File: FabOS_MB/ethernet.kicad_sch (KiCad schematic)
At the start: 42 parts, among them J1 RJ45, U4 LAN8742A, U5 USBLC6-4SC6, U6 CND-tek B1601S

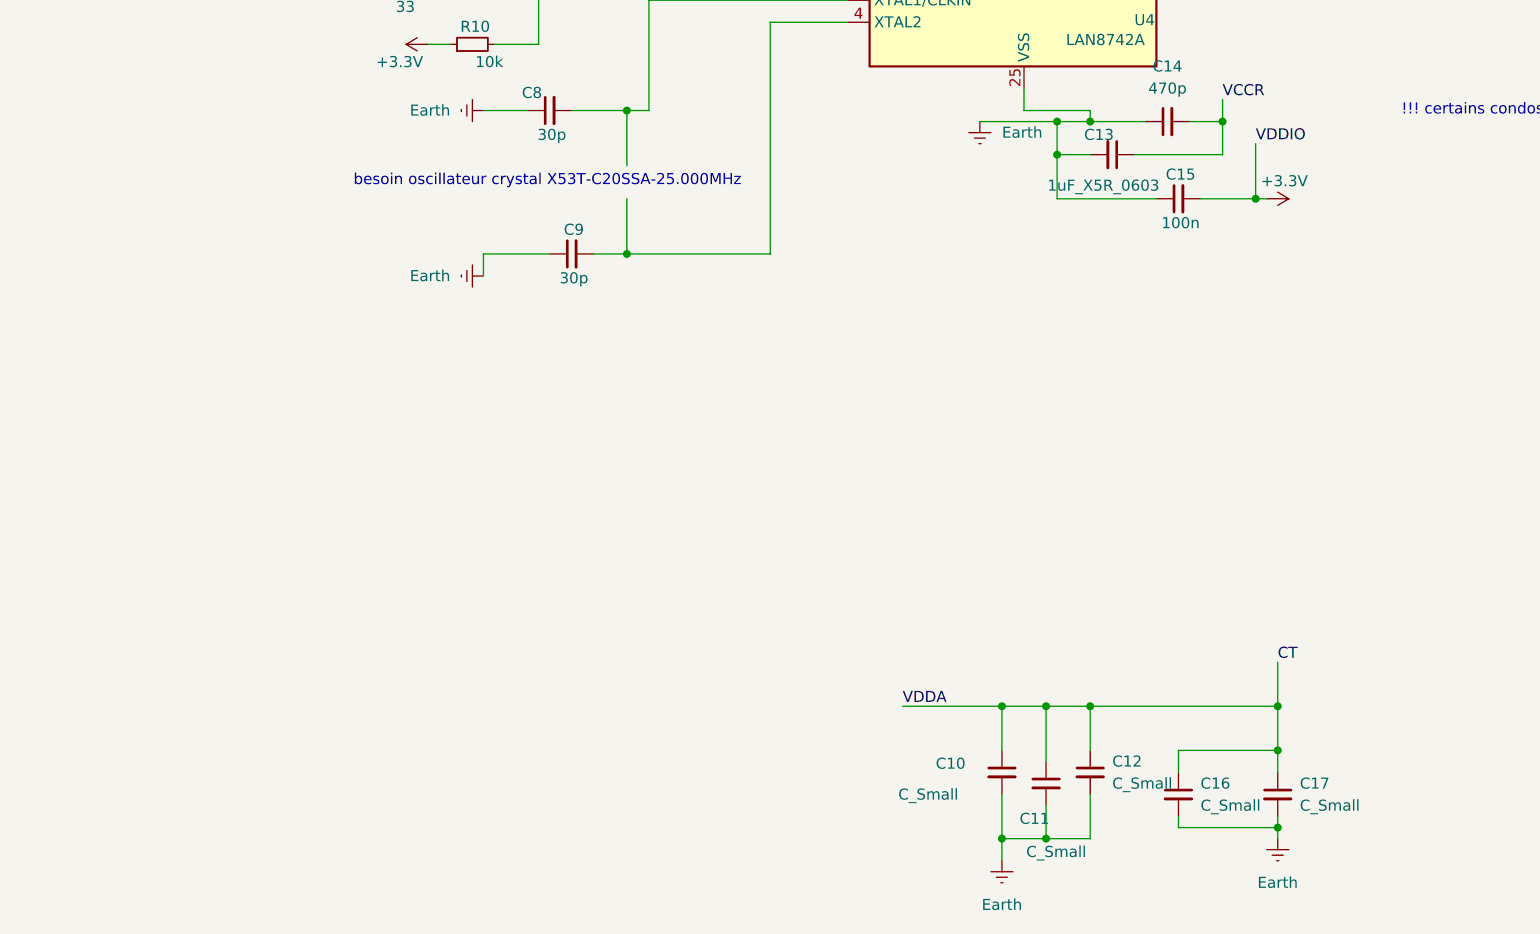
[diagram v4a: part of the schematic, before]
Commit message: ajout nom des composants pour 5v
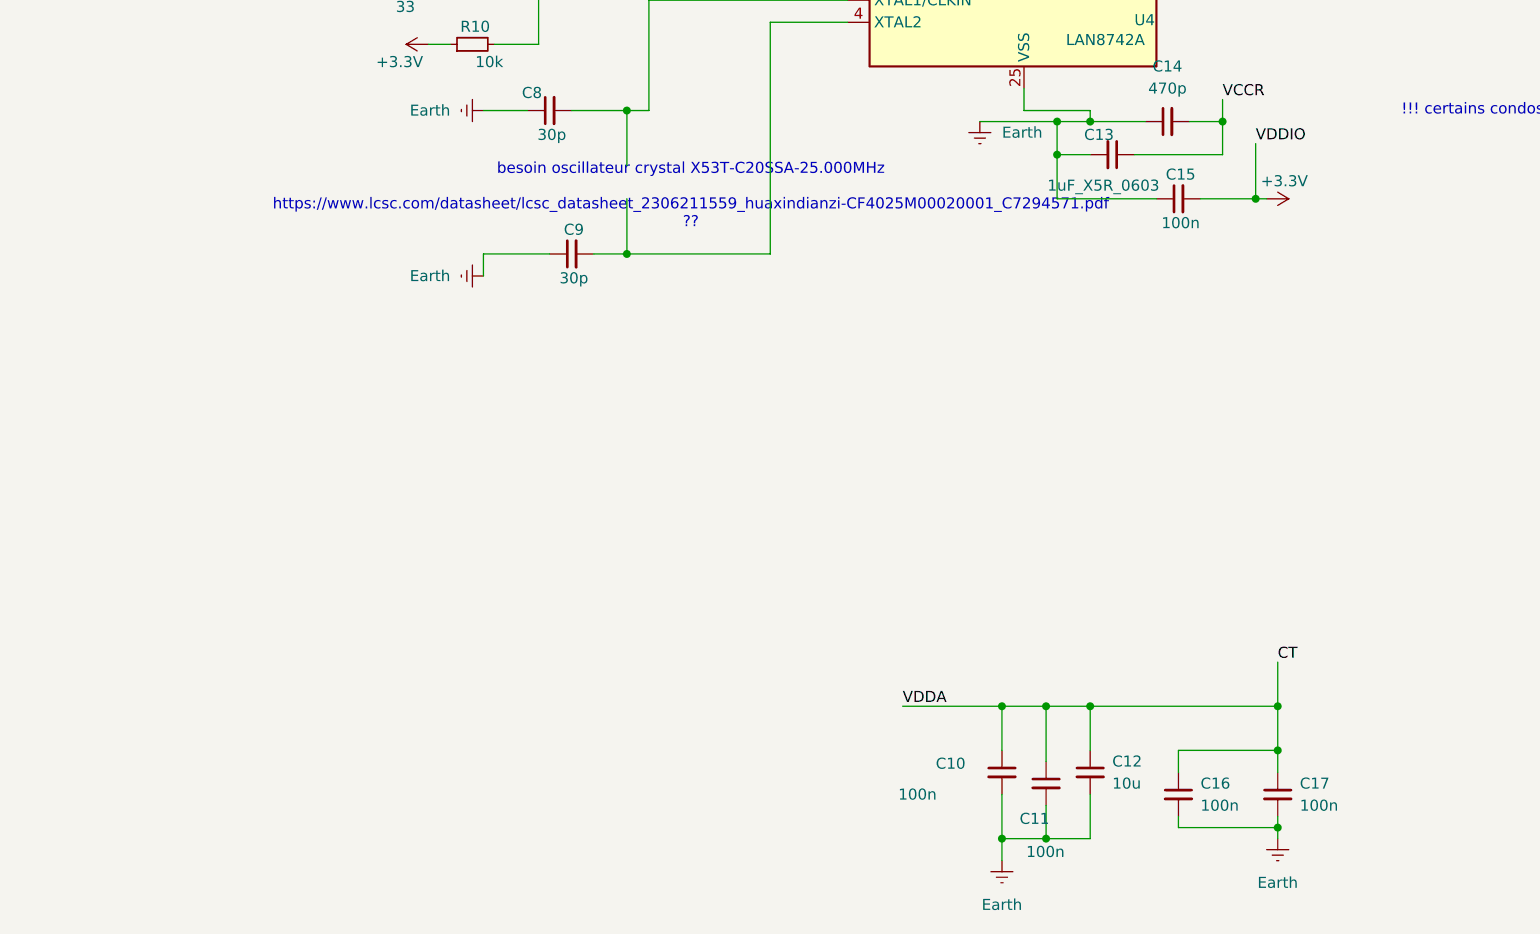
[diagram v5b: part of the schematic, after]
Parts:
- C10, C11, C16, C17: value C_Small -> 100n
- C12: value C_Small -> 10u
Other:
- note added: "besoin oscillateur crystal X53T-C20SSA-25.000MHz https://www.lcsc.com/datasheet/lcsc_datasheet_2306211559_huaxindianzi-CF4025M00020001_C7294571.pdf ??"
- note removed: "besoin oscillateur crystal X53T-C20SSA-25.000MHz"
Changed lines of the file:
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@@
 		)
 	)
-	(text "besoin oscillateur crystal X53T-C20SSA-25.000MHz"
+	(text "besoin oscillateur crystal X53T-C20SSA-25.000MHz\n\nhttps://www.lcsc.com/datasheet/lcsc_datasheet_2306211559_huaxindianzi-CF4025M00020001_C7294571.pdf \n??\n"
 		(exclude_from_sim no)
-		(at 74.676 103.378 0)
+		(at 91.186 105.156 0)
 		(effects
 			(font
@@
 			)
 		)
-		(property "Value" "C_Small"
+		(property "Value" "100n"
 			(at 129.794 180.594 0)
 			(effects
@@
 			)
 		)
-		(property "Value" "C_Small"
+		(property "Value" "100n"
 			(at 149.86 175.2662 0)
 			(effects
@@
 			)
 		)
-		(property "Value" "C_Small"
+		(property "Value" "100n"
 			(at 161.29 175.2662 0)
 			(effects
@@
 			)
 		)
-		(property "Value" "C_Small"
+		(property "Value" "10u"
 			(at 139.7 172.7262 0)
 			(effects
@@
 			)
 		)
-		(property "Value" "C_Small"
+		(property "Value" "100n"
 			(at 115.062 173.99 0)
 			(effects

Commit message: comopsants switch et ethernets fini?
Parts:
- added Y1: Crystal_GND24, Librairie_MB:Oscillateur crystal 4p, symbol Device:Crystal_GND24
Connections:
- net Earth: no longer C10.2, C11.2, C12.2, C13.2, C14.1, C15.1, C16.2, C17.2, C8.1, C9.1, JP2.2 (B), JP3.2 (B), R13.1, R18.2, R23.2, R24.2, R25.2, U4.25 (VSS)
- net at C9.2, U4.4 (XTAL2): now also Y1.1
- net at C8.2, U4.5 (XTAL1/CLKIN): now also Y1.3
- new net GND: C10.2, C11.2, C12.2, C13.2, C14.1, C15.1, C16.2, C17.2, C8.1, C9.1, JP2.2 (B), JP3.2 (B), R13.1, R18.2, R23.2, R24.2, R25.2, U4.25 (VSS), Y1.2, Y1.4
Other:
- note added: "besoin oscillateur crystal X53T-C20SSA-25.000MHz"
- note removed: "besoin oscillateur crystal X53T-C20SSA-25.000MHz https://www.lcsc.com/datasheet/lcsc_datasheet_2306211559_huaxindianzi-CF4025M00020001_C7294571.pdf ??"

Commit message: Correction de certaines erreurs
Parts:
- renumbered U4 to U3, U5 to U4, U6 to U5
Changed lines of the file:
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@@
 		(on_board yes)
 		(dnp no)
-		(property "Reference" "#PWR016"
+		(property "Reference" "#PWR019"
 			(at 62.23 69.85 0)
 			(effects
@@
 			(project "FabOS_MB"
 				(path "/09377d5d-727f-4ff4-92c8-7a0483d23f1e/97c1e665-4fec-464e-b9f4-4fa619e0ae43"
-					(reference "#PWR016")
+					(reference "#PWR019")
 					(unit 1)
 				)
@@
 		(dnp no)
 		(fields_autoplaced yes)
-		(property "Reference" "#PWR032"
+		(property "Reference" "#PWR031"
 			(at 172.72 67.31 0)
 			(effects
@@
 			(project ""
 				(path "/09377d5d-727f-4ff4-92c8-7a0483d23f1e/97c1e665-4fec-464e-b9f4-4fa619e0ae43"
-					(reference "#PWR032")
+					(reference "#PWR031")
 					(unit 1)
 				)
@@
 		(on_board yes)
 		(dnp no)
-		(property "Reference" "#PWR020"
+		(property "Reference" "#PWR024"
 			(at 81.28 21.59 0)
 			(effects
@@
 			(project "FabOS_MB"
 				(path "/09377d5d-727f-4ff4-92c8-7a0483d23f1e/97c1e665-4fec-464e-b9f4-4fa619e0ae43"
-					(reference "#PWR020")
+					(reference "#PWR024")
 					(unit 1)
 				)
@@
 		(dnp no)
 		(fields_autoplaced yes)
-		(property "Reference" "#PWR023"
+		(property "Reference" "#PWR028"
 			(at 127 187.96 0)
 			(effects
@@
 			(project "FabOS_MB"
 				(path "/09377d5d-727f-4ff4-92c8-7a0483d23f1e/97c1e665-4fec-464e-b9f4-4fa619e0ae43"
-					(reference "#PWR023")
+					(reference "#PWR028")
 					(unit 1)
 				)
@@
 		(dnp no)
 		(fields_autoplaced yes)
-		(property "Reference" "#PWR026"
+		(property "Reference" "#PWR036"
 			(at 276.86 120.65 0)
 			(effects
@@
 			(project "FabOS_MB"
 				(path "/09377d5d-727f-4ff4-92c8-7a0483d23f1e/97c1e665-4fec-464e-b9f4-4fa619e0ae43"
-					(reference "#PWR026")
+					(reference "#PWR036")
 					(unit 1)
 				)
@@
 		(on_board yes)
 		(dnp no)
-		(property "Reference" "#PWR028"
+		(property "Reference" "#PWR033"
 			(at 189.23 20.32 0)
 			(effects
@@
 			(project "FabOS_MB"
 				(path "/09377d5d-727f-4ff4-92c8-7a0483d23f1e/97c1e665-4fec-464e-b9f4-4fa619e0ae43"
-					(reference "#PWR028")
+					(reference "#PWR033")
 					(unit 1)
 				)
@@
 		(dnp no)
 		(fields_autoplaced yes)
-		(property "Reference" "#PWR030"
+		(property "Reference" "#PWR035"
 			(at 224.79 114.3 0)
 			(effects
@@
 			(project "FabOS_MB"
 				(path "/09377d5d-727f-4ff4-92c8-7a0483d23f1e/97c1e665-4fec-464e-b9f4-4fa619e0ae43"
-					(reference "#PWR030")
+					(reference "#PWR035")
 					(unit 1)
 				)
@@
 		(dnp no)
 		(fields_autoplaced yes)
-		(property "Reference" "#PWR025"
+		(property "Reference" "#PWR021"
 			(at 60.96 95.25 0)
 			(effects
@@
 			(project "FabOS_MB"
 				(path "/09377d5d-727f-4ff4-92c8-7a0483d23f1e/97c1e665-4fec-464e-b9f4-4fa619e0ae43"
-					(reference "#PWR025")
+					(reference "#PWR021")
 					(unit 1)
 				)
@@
 		(dnp no)
 		(fields_autoplaced yes)
-		(property "Reference" "#PWR031"
+		(property "Reference" "#PWR027"
 			(at 124.46 102.87 0)
 			(effects
@@
 			(project "FabOS_MB"
 				(path "/09377d5d-727f-4ff4-92c8-7a0483d23f1e/97c1e665-4fec-464e-b9f4-4fa619e0ae43"
-					(reference "#PWR031")
+					(reference "#PWR027")
 					(unit 1)
 				)
@@
 		(dnp no)
 		(fields_autoplaced yes)
-		(property "Reference" "#PWR018"
+		(property "Reference" "#PWR022"
 			(at 67.31 120.65 0)
 			(effects
@@
 			(project "FabOS_MB"
 				(path "/09377d5d-727f-4ff4-92c8-7a0483d23f1e/97c1e665-4fec-464e-b9f4-4fa619e0ae43"
-					(reference "#PWR018")
+					(reference "#PWR022")
 					(unit 1)
 				)
@@
 		(dnp no)
 		(fields_autoplaced yes)
-		(property "Reference" "#PWR021"
+		(property "Reference" "#PWR025"
 			(at 77.47 62.23 0)
 			(effects
@@
 			(project "FabOS_MB"
 				(path "/09377d5d-727f-4ff4-92c8-7a0483d23f1e/97c1e665-4fec-464e-b9f4-4fa619e0ae43"
-					(reference "#PWR021")
+					(reference "#PWR025")
 					(unit 1)
 				)
@@
 		(on_board yes)
 		(dnp no)
-		(property "Reference" "#PWR024"
+		(property "Reference" "#PWR029"
 			(at 153.67 105.41 0)
 			(effects
@@
 			(project "FabOS_MB"
 				(path "/09377d5d-727f-4ff4-92c8-7a0483d23f1e/97c1e665-4fec-464e-b9f4-4fa619e0ae43"
-					(reference "#PWR024")
+					(reference "#PWR029")
 					(unit 1)
 				)
@@
 		(on_board yes)
 		(dnp no)
-		(property "Reference" "#PWR027"
+		(property "Reference" "#PWR032"
 			(at 161.29 34.29 0)
 			(effects
@@
 			(project "FabOS_MB"
 				(path "/09377d5d-727f-4ff4-92c8-7a0483d23f1e/97c1e665-4fec-464e-b9f4-4fa619e0ae43"
-					(reference "#PWR027")
+					(reference "#PWR032")
 					(unit 1)
 				)
@@
 		(on_board yes)
 		(dnp no)
-		(property "Reference" "U5"
+		(property "Reference" "U4"
 			(at 177.8 24.13 90)
 			(effects
@@
 			(project "FabOS_MB"
 				(path "/09377d5d-727f-4ff4-92c8-7a0483d23f1e/97c1e665-4fec-464e-b9f4-4fa619e0ae43"
-					(reference "U5")
+					(reference "U4")
 					(unit 1)
 				)
@@
 		(dnp no)
 		(fields_autoplaced yes)
-		(property "Reference" "#PWR033"
+		(property "Reference" "#PWR026"
 			(at 95.25 104.14 0)
 			(effects
@@
 			(project "FabOS_MB"
 				(path "/09377d5d-727f-4ff4-92c8-7a0483d23f1e/97c1e665-4fec-464e-b9f4-4fa619e0ae43"
-					(reference "#PWR033")
+					(reference "#PWR026")
 					(unit 1)
 				)
@@
 		(dnp no)
 		(fields_autoplaced yes)
-		(property "Reference" "#PWR029"
+		(property "Reference" "#PWR034"
 			(at 210.82 34.29 0)
 			(effects
@@
 			(project "FabOS_MB"
 				(path "/09377d5d-727f-4ff4-92c8-7a0483d23f1e/97c1e665-4fec-464e-b9f4-4fa619e0ae43"
-					(reference "#PWR029")
+					(reference "#PWR034")
 					(unit 1)
 				)
@@
 		(on_board yes)
 		(dnp no)
-		(property "Reference" "U6"
+		(property "Reference" "U5"
 			(at 208.5975 40.64 0)
 			(effects
@@
 			(project "FabOS_MB"
 				(path "/09377d5d-727f-4ff4-92c8-7a0483d23f1e/97c1e665-4fec-464e-b9f4-4fa619e0ae43"
-					(reference "U6")
+					(reference "U5")
 					(unit 1)
 				)
@@
 		(dnp no)
 		(fields_autoplaced yes)
-		(property "Reference" "#PWR019"
+		(property "Reference" "#PWR023"
 			(at 72.39 104.14 0)
 			(effects
@@
 			(project "FabOS_MB"
 				(path "/09377d5d-727f-4ff4-92c8-7a0483d23f1e/97c1e665-4fec-464e-b9f4-4fa619e0ae43"
-					(reference "#PWR019")
+					(reference "#PWR023")
 					(unit 1)
 				)
@@
 		(dnp no)
 		(fields_autoplaced yes)
-		(property "Reference" "#PWR022"
+		(property "Reference" "#PWR030"
 			(at 158.75 185.42 0)
 			(effects
@@
 			(project "FabOS_MB"
 				(path "/09377d5d-727f-4ff4-92c8-7a0483d23f1e/97c1e665-4fec-464e-b9f4-4fa619e0ae43"
-					(reference "#PWR022")
+					(reference "#PWR030")
 					(unit 1)
 				)
@@
 		(on_board yes)
 		(dnp no)
-		(property "Reference" "U4"
+		(property "Reference" "U3"
 			(at 142.24 84.836 0)
 			(effects
@@
 			(project "FabOS_MB"
 				(path "/09377d5d-727f-4ff4-92c8-7a0483d23f1e/97c1e665-4fec-464e-b9f4-4fa619e0ae43"
-					(reference "U4")
+					(reference "U3")
 					(unit 1)
 				)
@@
 		(on_board yes)
 		(dnp no)
-		(property "Reference" "#PWR017"
+		(property "Reference" "#PWR020"
 			(at 64.77 87.63 0)
 			(effects
@@
 			(project "FabOS_MB"
 				(path "/09377d5d-727f-4ff4-92c8-7a0483d23f1e/97c1e665-4fec-464e-b9f4-4fa619e0ae43"
-					(reference "#PWR017")
+					(reference "#PWR020")
 					(unit 1)
 				)

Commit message: Il ne reste plus qu'a router
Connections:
- net GNDPWR is gone; now on net GND: C19.2, JP2.1 (A), JP3.1 (A)
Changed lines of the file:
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@@
 	(wire
 		(pts
+			(xy 233.68 58.42) (xy 233.68 85.09)
+		)
+		(stroke
+			(width 0)
+			(type default)
+		)
+	)
+	(wire
+		(pts
 			(xy 269.24 50.8) (xy 275.59 50.8)
 		)
@@
 	(wire
 		(pts
+			(xy 238.76 66.04) (xy 238.76 85.09)
+		)
+		(stroke
+			(width 0)
+			(type default)
+		)
+	)
+	(wire
+		(pts
 			(xy 147.32 168.91) (xy 158.75 168.91)
 		)
@@
 	(wire
 		(pts
-			(xy 233.68 58.42) (xy 233.68 85.09)
-		)
-		(stroke
-			(width 0)
-			(type default)
-		)
-	)
-	(wire
-		(pts
 			(xy 229.87 52.07) (xy 243.84 52.07)
 		)
@@
 	(wire
 		(pts
+			(xy 223.52 72.39) (xy 226.06 72.39)
+		)
+		(stroke
+			(width 0)
+			(type default)
+		)
+	)
+	(wire
+		(pts
 			(xy 170.18 59.69) (xy 147.32 59.69)
 		)
@@
 	(wire
 		(pts
-			(xy 238.76 66.04) (xy 238.76 85.09)
-		)
-		(stroke
-			(width 0)
-			(type default)
-		)
-	)
-	(wire
-		(pts
 			(xy 106.68 44.45) (xy 29.21 44.45)
 		)
@@
 	(wire
 		(pts
-			(xy 226.06 72.39) (xy 223.52 72.39)
-		)
-		(stroke
-			(width 0)
-			(type default)
-		)
-	)
-	(wire
-		(pts
 			(xy 77.47 95.25) (xy 83.82 95.25)
 		)
@@
 	)
 	(symbol
-		(lib_id "power:GNDPWR")
-		(at 224.79 109.22 0)
-		(unit 1)
-		(exclude_from_sim no)
-		(in_bom yes)
-		(on_board yes)
-		(dnp no)
-		(fields_autoplaced yes)
-		(property "Reference" "#PWR035"
-			(at 224.79 114.3 0)
-			(effects
-				(font
-					(size 1.27 1.27)
-				)
-				(hide yes)
-			)
-		)
-		(property "Value" "GNDPWR"
-			(at 224.663 113.03 0)
-			(effects
-				(font
-					(size 1.27 1.27)
-				)
-			)
-		)
-		(property "Footprint" ""
-			(at 224.79 110.49 0)
-			(effects
-				(font
-					(size 1.27 1.27)
-				)
-				(hide yes)
-			)
-		)
-		(property "Datasheet" ""
-			(at 224.79 110.49 0)
-			(effects
-				(font
-					(size 1.27 1.27)
-				)
-				(hide yes)
-			)
-		)
-		(property "Description" "Power symbol creates a global label with name \"GNDPWR\" , global ground"
-			(at 224.79 109.22 0)
-			(effects
-				(font
-					(size 1.27 1.27)
-				)
-				(hide yes)
-			)
-		)
-		(pin "1"
-		)
-		(instances
-			(project "FabOS_MB"
-				(path "/09377d5d-727f-4ff4-92c8-7a0483d23f1e/97c1e665-4fec-464e-b9f4-4fa619e0ae43"
-					(reference "#PWR035")
-					(unit 1)
-				)
-			)
-		)
-	)
-	(symbol
 		(lib_id "power:GND")
 		(at 67.31 95.25 270)
@@
 					(unit 1)
 				)
+			)
+		)
+	)
+	(symbol
+		(lib_id "power:GND")
+		(at 224.79 109.22 0)
+		(unit 1)
+		(exclude_from_sim no)
+		(in_bom yes)
+		(on_board yes)
+		(dnp no)
+		(fields_autoplaced yes)
+		(property "Reference" "#PWR08"
+			(at 224.79 115.57 0)
+			(effects
+				(font
+					(size 1.27 1.27)
+				)
+				(hide yes)
+			)
+		)
+		(property "Value" "GND"
+			(at 224.79 114.3 0)
+			(effects
+				(font
+					(size 1.27 1.27)
+				)
+			)
+		)
+		(property "Footprint" ""
+			(at 224.79 109.22 0)
+			(effects
+				(font
+					(size 1.27 1.27)
+				)
+				(hide yes)
+			)
+		)
+		(property "Datasheet" ""
+			(at 224.79 109.22 0)
+			(effects
+				(font
+					(size 1.27 1.27)
+				)
+				(hide yes)
+			)
+		)
+		(property "Description" "Power symbol creates a global label with name \"GND\" , ground"
+			(at 224.79 109.22 0)
+			(effects
+				(font
+					(size 1.27 1.27)
+				)
+				(hide yes)
+			)
+		)
+		(pin "1"
+		)
+		(instances
+			(project ""
+				(path "/09377d5d-727f-4ff4-92c8-7a0483d23f1e/97c1e665-4fec-464e-b9f4-4fa619e0ae43"
+					(reference "#PWR08")
+					(unit 1)
+				)
